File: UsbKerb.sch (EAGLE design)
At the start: 23 parts, among them IC1 XMEGA16A4A, U1 UA78M33CDCY, U2 3.3TVS

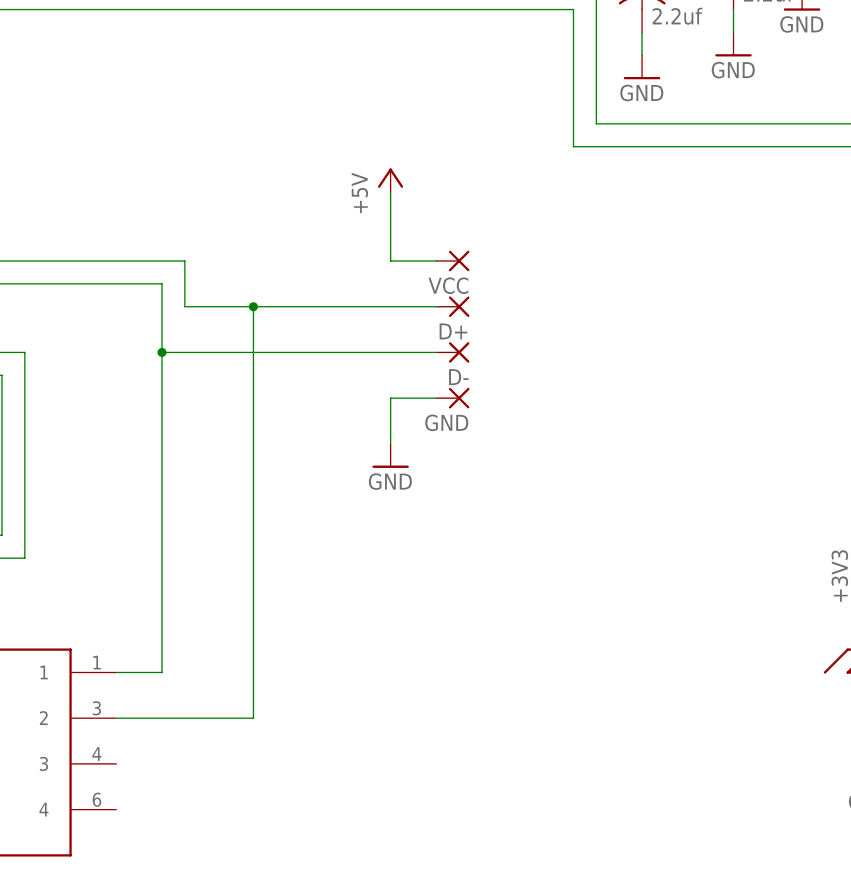
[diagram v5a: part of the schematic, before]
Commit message: Swapped USB Pads for USB Mini connector
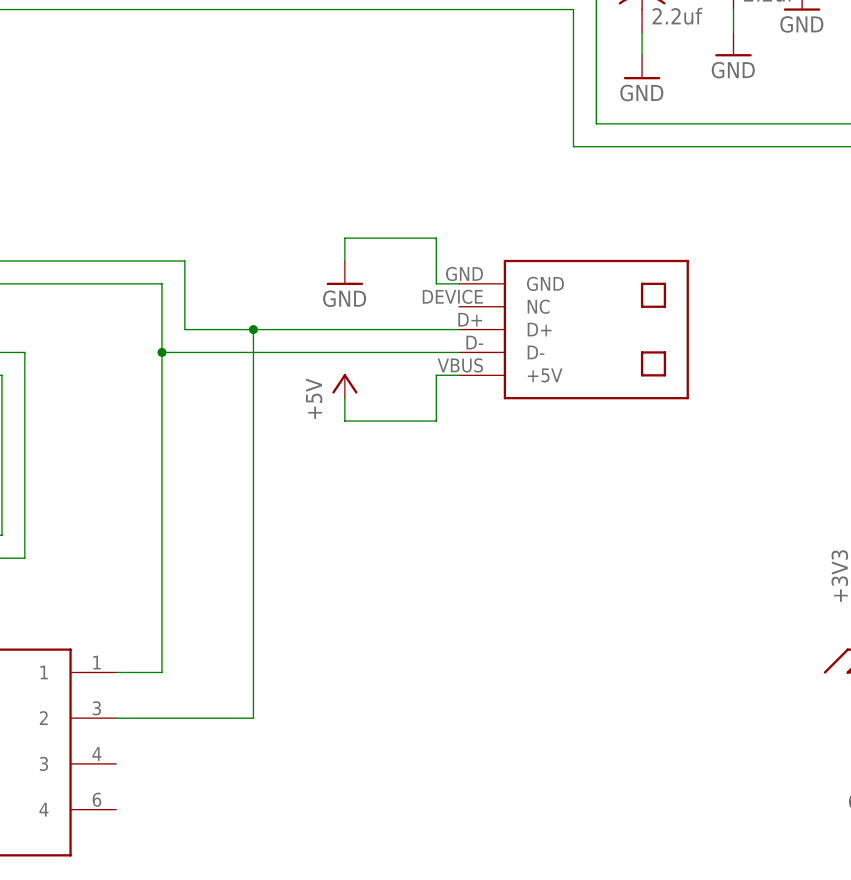
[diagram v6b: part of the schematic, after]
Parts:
- removed D+, D-, GND, VCC: (no value), wirepad:3,81/1,4
- added U$1: USB-MINI, usb:USB-MINI
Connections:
- net +5V: now also U$1.+5V; no longer VCC.P
- net GND: now also U$1.GND; no longer GND.P
- net N$2: now also U$1.D+; no longer D+.P
- net N$4: now also U$1.D-; no longer D-.P
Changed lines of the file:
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@@
 <?xml version="1.0" encoding="utf-8"?>
 <!DOCTYPE eagle SYSTEM "eagle.dtd">
-<eagle version="7.2.0">
+<eagle version="7.5.0">
 <drawing>
 <settings>
@@
 <parts>
 <part name="IC1" library="atmel" deviceset="XMEGA16A4" device="A"/>
-<part name="VCC" library="wirepad" deviceset="3,81/1,4" device=""/>
-<part name="D+" library="wirepad" deviceset="3,81/1,4" device=""/>
-<part name="D-" library="wirepad" deviceset="3,81/1,4" device=""/>
-<part name="GND" library="wirepad" deviceset="3,81/1,4" device=""/>
 <part name="JP1" library="pinhead" deviceset="PINHD-2X6" device=""/>
 <part name="R3" library="resistor" deviceset="R-US_" device="R0805W" value="22K"/>
@@
 <part name="C6" library="rcl" deviceset="CPOL-US" device="G" value="470uf"/>
 <part name="JP2" library="pinhead" deviceset="PINHD-2X3" device=""/>
-<part name="P+8" library="supply1" deviceset="+5V" device=""/>
 <part name="GND12" library="supply1" deviceset="GND" device=""/>
 <part name="+3V1" library="supply1" deviceset="+3V3" device=""/>
@@
 <part name="+3V6" library="supply1" deviceset="+3V3" device=""/>
 <part name="C7" library="resistor" deviceset="C-EU" device="C1206K"/>
+<part name="U$1" library="usb" deviceset="USB-MINI" device=""/>
+<part name="P+2" library="supply1" deviceset="+5V" device=""/>
 </parts>
 <sheets>
@@
 <instances>
 <instance part="IC1" gate="G$1" x="66.04" y="50.8"/>
-<instance part="VCC" gate="1" x="149.86" y="30.48" rot="R180"/>
-<instance part="D+" gate="1" x="149.86" y="25.4" rot="R180"/>
-<instance part="D-" gate="1" x="149.86" y="20.32" rot="R180"/>
-<instance part="GND" gate="1" x="149.86" y="15.24" rot="R180"/>
 <instance part="JP1" gate="A" x="269.24" y="68.58"/>
 <instance part="R3" gate="G$1" x="198.12" y="86.36"/>
@@
 <instance part="GND2" gate="1" x="180.34" y="53.34"/>
 <instance part="GND3" gate="1" x="170.18" y="50.8"/>
-<instance part="GND4" gate="1" x="142.24" y="7.62"/>
+<instance part="GND4" gate="1" x="137.16" y="27.94"/>
 <instance part="GND5" gate="1" x="-27.94" y="73.66"/>
 <instance part="GND6" gate="1" x="289.56" y="50.8"/>
 <instance part="GND7" gate="1" x="251.46" y="50.8"/>
 <instance part="GND8" gate="1" x="27.94" y="43.18"/>
-<instance part="P+1" gate="1" x="142.24" y="40.64"/>
+<instance part="P+1" gate="1" x="137.16" y="17.78"/>
 <instance part="C1" gate="G$1" x="187.96" y="68.58"/>
 <instance part="C2" gate="G$1" x="180.34" y="63.5"/>
@@
 <instance part="C6" gate="G$1" x="210.82" y="-12.7"/>
 <instance part="JP2" gate="A" x="45.72" y="-22.86"/>
-<instance part="P+8" gate="1" x="35.56" y="-12.7"/>
 <instance part="GND12" gate="1" x="63.5" y="-15.24"/>
 <instance part="+3V1" gate="G$1" x="256.54" y="86.36"/>
@@
 <instance part="+3V6" gate="G$1" x="-27.94" y="99.06"/>
 <instance part="C7" gate="G$1" x="220.98" y="-12.7"/>
+<instance part="U$1" gate="G$1" x="162.56" y="22.86" smashed="yes" rot="R90"/>
+<instance part="P+2" gate="1" x="35.56" y="-12.7"/>
 </instances>
 <busses>
@@
 <segment>
 <pinref part="IC1" gate="G$1" pin="PD7"/>
-<pinref part="D+" gate="1" pin="P"/>
-<wire x1="119.38" y1="25.4" x2="127" y2="25.4" width="0.1524" layer="91"/>
-<wire x1="127" y1="25.4" x2="147.32" y2="25.4" width="0.1524" layer="91"/>
-<wire x1="119.38" y1="30.48" x2="119.38" y2="25.4" width="0.1524" layer="91"/>
+<wire x1="119.38" y1="22.86" x2="127" y2="22.86" width="0.1524" layer="91"/>
+<wire x1="127" y1="22.86" x2="149.86" y2="22.86" width="0.1524" layer="91"/>
+<wire x1="119.38" y1="30.48" x2="119.38" y2="22.86" width="0.1524" layer="91"/>
 <wire x1="93.98" y1="30.48" x2="119.38" y2="30.48" width="0.1524" layer="91"/>
-<wire x1="127" y1="-20.32" x2="127" y2="25.4" width="0.1524" layer="91"/>
-<junction x="127" y="25.4"/>
+<wire x1="127" y1="-20.32" x2="127" y2="22.86" width="0.1524" layer="91"/>
+<junction x="127" y="22.86"/>
 <pinref part="U2" gate="G$1" pin="2"/>
 <wire x1="127" y1="-20.32" x2="111.76" y2="-20.32" width="0.1524" layer="91"/>
+<pinref part="U$1" gate="G$1" pin="D+"/>
 </segment>
 </net>
 <net name="N$4" class="0">
 <segment>
-<pinref part="D-" gate="1" pin="P"/>
-<wire x1="116.84" y1="20.32" x2="147.32" y2="20.32" width="0.1524" layer="91"/>
+<wire x1="116.84" y1="20.32" x2="149.86" y2="20.32" width="0.1524" layer="91"/>
 <wire x1="116.84" y1="27.94" x2="116.84" y2="20.32" width="0.1524" layer="91"/>
 <pinref part="IC1" gate="G$1" pin="PD6"/>
@@
 <pinref part="U2" gate="G$1" pin="1"/>
 <wire x1="116.84" y1="-15.24" x2="111.76" y2="-15.24" width="0.1524" layer="91"/>
+<pinref part="U$1" gate="G$1" pin="D-"/>
 </segment>
 </net>
 <net name="GND" class="0">
 <segment>
-<pinref part="GND" gate="1" pin="P"/>
-<wire x1="142.24" y1="15.24" x2="147.32" y2="15.24" width="0.1524" layer="91"/>
+<wire x1="137.16" y1="33.02" x2="147.32" y2="33.02" width="0.1524" layer="91"/>
 <pinref part="GND4" gate="1" pin="GND"/>
-<wire x1="142.24" y1="15.24" x2="142.24" y2="10.16" width="0.1524" layer="91"/>
+<wire x1="137.16" y1="33.02" x2="137.16" y2="30.48" width="0.1524" layer="91"/>
+<wire x1="147.32" y1="33.02" x2="147.32" y2="27.94" width="0.1524" layer="91"/>
+<pinref part="U$1" gate="G$1" pin="GND"/>
+<wire x1="147.32" y1="27.94" x2="149.86" y2="27.94" width="0.1524" layer="91"/>
 </segment>
 <segment>
@@
 <net name="+5V" class="0">
 <segment>
-<pinref part="VCC" gate="1" pin="P"/>
 <pinref part="P+1" gate="1" pin="+5V"/>
-<wire x1="147.32" y1="30.48" x2="142.24" y2="30.48" width="0.1524" layer="91"/>
-<wire x1="142.24" y1="30.48" x2="142.24" y2="38.1" width="0.1524" layer="91"/>
-</segment>
-<segment>
-<pinref part="JP2" gate="A" pin="1"/>
-<pinref part="P+8" gate="1" pin="+5V"/>
-<wire x1="43.18" y1="-20.32" x2="35.56" y2="-20.32" width="0.1524" layer="91"/>
-<wire x1="35.56" y1="-20.32" x2="35.56" y2="-15.24" width="0.1524" layer="91"/>
+<wire x1="147.32" y1="12.7" x2="137.16" y2="12.7" width="0.1524" layer="91"/>
+<wire x1="137.16" y1="12.7" x2="137.16" y2="15.24" width="0.1524" layer="91"/>
+<wire x1="147.32" y1="12.7" x2="147.32" y2="17.78" width="0.1524" layer="91"/>
+<pinref part="U$1" gate="G$1" pin="+5V"/>
+<wire x1="147.32" y1="17.78" x2="149.86" y2="17.78" width="0.1524" layer="91"/>
 </segment>
 <segment>
@@
 <wire x1="281.94" y1="-7.62" x2="274.32" y2="-7.62" width="0.1524" layer="91"/>
 </segment>
+<segment>
+<pinref part="JP2" gate="A" pin="1"/>
+<wire x1="43.18" y1="-20.32" x2="35.56" y2="-20.32" width="0.1524" layer="91"/>
+<wire x1="35.56" y1="-20.32" x2="35.56" y2="-15.24" width="0.1524" layer="91"/>
+<pinref part="P+2" gate="1" pin="+5V"/>
+</segment>
 </net>
